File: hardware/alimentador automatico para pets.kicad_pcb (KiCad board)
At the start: 2 copper layers, 96 x 90 mm, 31 parts, among them J1 Conn_01x02, J2 Conn_01x04, J3 Conn_01x03, J4 Conn_01x03, J5 Conn_01x02, J6 Conn_01x05, J7 Conn_01x02, J8 Conn_01x04, Q1 BC337, SW1 SW_Push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

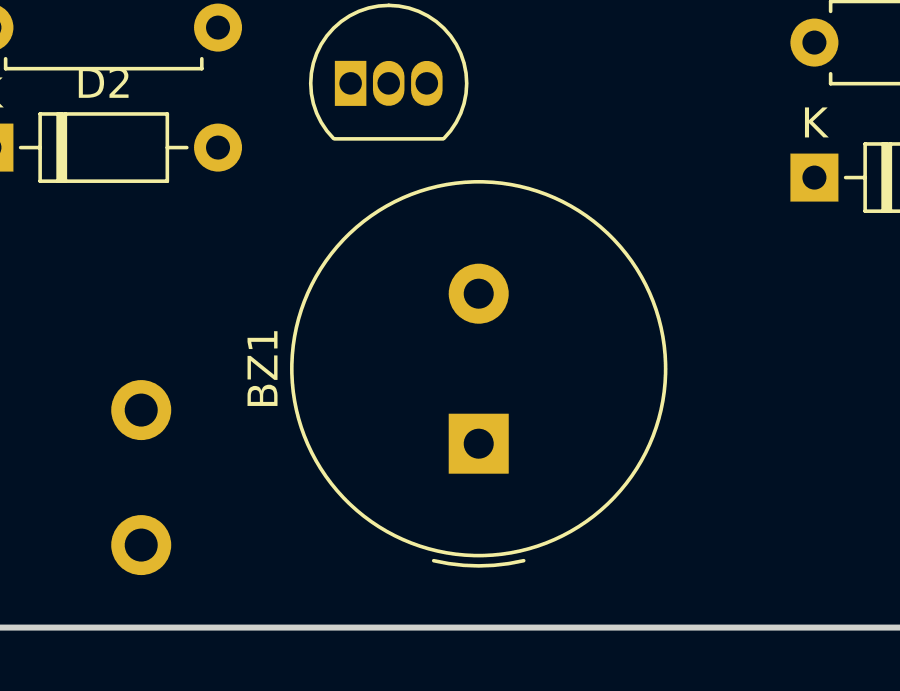
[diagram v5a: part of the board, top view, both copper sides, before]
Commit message: add 3d models pins #14
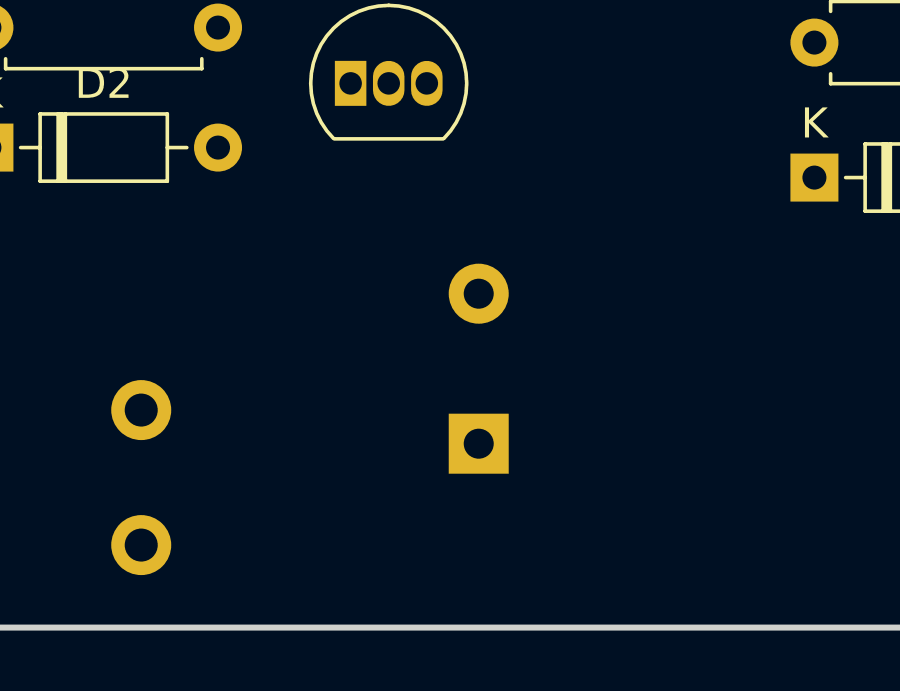
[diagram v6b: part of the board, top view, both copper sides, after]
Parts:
- BZ1: moved to B.Cu
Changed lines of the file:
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@@
-    )
-  )
-  (footprint "Buzzer_Beeper:Buzzer_TDK_PS1240P02BT_D12.2mm_H6.5mm" (layer "F.Cu")
-    (at 89.5 108.870785 90)
-    (descr "Buzzer, D12.2mm height 6.5mm, https://product.tdk.com/info/en/catalog/datasheets/piezoelectronic_buzzer_ps_en.pdf")
-    (tags "buzzer")
-    (property "Sheetfile" "alimentador automatico para pets.kicad_sch")
-    (property "Sheetname" "")
-    (attr through_hole)
-    (fp_text reference "BZ1" (at 2.5 -7.17 90) (layer "F.SilkS")
-      (effects (font (size 1 1) (thickness 0.15)))
-    )
-    (fp_text value "Buzzer" (at 2.5 7.31 90) (layer "F.Fab")
-      (effects (font (size 1 1) (thickness 0.15)))
-    )
-    (fp_text user "${REFERENCE}" (at 2.5 -2.43 90) (layer "F.Fab")
-      (effects (font (size 1 1) (thickness 0.15)))
-    )
-    (fp_arc (start -3.9 1.499999) (mid -4.073431 -0.000001) (end -3.9 -1.5) (layer "F.SilkS") (width 0.12))
-    (fp_circle (center 2.5 0) (end 8.73 0) (layer "F.SilkS") (width 0.12) (fill none))
-    (fp_circle (center 2.5 0) (end 8.85 0) (layer "F.CrtYd") (width 0.05) (fill none))
-    (fp_line (start -1.3 -1) (end -1.3 1) (layer "F.Fab") (width 0.1))
-    (fp_circle (center 2.5 0) (end 3.5 0) (layer "F.Fab") (width 0.1) (fill none))
-    (fp_circle (center 2.5 0) (end 8.6 0) (layer "F.Fab") (width 0.1) (fill none))
-    (pad "1" thru_hole rect (at 0 0 90) (size 2 2) (drill 1) (layers *.Cu *.Mask)
-      (net 1 "/5V") (pinfunction "-") (pintype "passive"))
-    (pad "2" thru_hole circle (at 5 0 90) (size 2 2) (drill 1) (layers *.Cu *.Mask)
-      (net 8 "Net-(BZ1-Pad2)") (pinfunction "+") (pintype "passive"))
-    (model "${KICAD6_3DMODEL_DIR}/Buzzer_Beeper.3dshapes/Buzzer_TDK_PS1240P02BT_D12.2mm_H6.5mm.wrl"
-      (offset (xyz 0 0 0))
-      (scale (xyz 1 1 1))
-      (rotate (xyz 0 0 0))
     )
   )
@@
       (net 13 "/red_wire") (pinfunction "+E") (pintype "input"))
     (model "${KIPRJMOD}/3d_models/HX711.STEP"
-      (offset (xyz 18 10.5 2))
+      (offset (xyz 18.5 10.3 2.5))
       (scale (xyz 1 1 1))
       (rotate (xyz 0 0 180))
+    )
+    (model "${KICAD6_3DMODEL_DIR}/Connector_PinHeader_2.54mm.3dshapes/PinHeader_1x04_P2.54mm_Vertical.step"
+      (offset (xyz -11 4 2.5))
+      (scale (xyz 1 1 1))
+      (rotate (xyz 0 -180 0))
+    )
+    (model "${KICAD6_3DMODEL_DIR}/Connector_PinHeader_2.54mm.3dshapes/PinHeader_1x06_P2.54mm_Vertical.step"
+      (offset (xyz 14 6.3 2))
+      (scale (xyz 1 1 1))
+      (rotate (xyz 0 180 0))
     )
   )
@@
     )
   )
+  (footprint "Buzzer_Beeper:Buzzer_TDK_PS1240P02BT_D12.2mm_H6.5mm" (layer "B.Cu")
+    (at 89.5 108.870785 90)
+    (descr "Buzzer, D12.2mm height 6.5mm, https://product.tdk.com/info/en/catalog/datasheets/piezoelectronic_buzzer_ps_en.pdf")
+    (tags "buzzer")
+    (property "Sheetfile" "alimentador automatico para pets.kicad_sch")
+    (property "Sheetname" "")
+    (attr through_hole)
+    (fp_text reference "BZ1" (at 2.5 7.17 90) (layer "B.SilkS")
+      (effects (font (size 1 1) (thickness 0.15)) (justify mirror))
+    )
+    (fp_text value "Buzzer" (at 2.5 -7.31 90) (layer "B.Fab")
+      (effects (font (size 1 1) (thickness 0.15)) (justify mirror))
+    )
+    (fp_text user "${REFERENCE}" (at 2.5 2.43 90) (layer "B.Fab")
+      (effects (font (size 1 1) (thickness 0.15)) (justify mirror))
+    )
+    (fp_arc (start -3.9 1.5) (mid -4.073431 0.000001) (end -3.9 -1.499999) (layer "B.SilkS") (width 0.12))
+    (fp_circle (center 2.5 0) (end 8.73 0) (layer "B.SilkS") (width 0.12) (fill none))
+    (fp_circle (center 2.5 0) (end 8.85 0) (layer "B.CrtYd") (width 0.05) (fill none))
+    (fp_line (start -1.3 1) (end -1.3 -1) (layer "B.Fab") (width 0.1))
+    (fp_circle (center 2.5 0) (end 3.5 0) (layer "B.Fab") (width 0.1) (fill none))
+    (fp_circle (center 2.5 0) (end 8.6 0) (layer "B.Fab") (width 0.1) (fill none))
+    (pad "1" thru_hole rect (at 0 0 90) (size 2 2) (drill 1) (layers *.Cu *.Mask)
+      (net 1 "/5V") (pinfunction "-") (pintype "passive"))
+    (pad "2" thru_hole circle (at 5 0 90) (size 2 2) (drill 1) (layers *.Cu *.Mask)
+      (net 8 "Net-(BZ1-Pad2)") (pinfunction "+") (pintype "passive"))
+    (model "${KICAD6_3DMODEL_DIR}/Buzzer_Beeper.3dshapes/Buzzer_TDK_PS1240P02BT_D12.2mm_H6.5mm.wrl"
+      (offset (xyz 0 0 0))
+      (scale (xyz 1 1 1))
+      (rotate (xyz 0 0 0))
+    )
+  )
   (footprint "Button_Switch_THT:SW_PUSH_6mm" (layer "B.Cu")
     (at 53.25 107.75 180)
@@
     (effects (font (size 1.5 1.5) (thickness 0.3)))
   )
+  (dimension (type aligned) (layer "Edge.Cuts")
+    (pts (xy 38.5 99.25) (xy 38.5 103))
+    (height 0)
+    (gr_text "3.7500 mm" (at 37.35 101.125 90) (layer "Edge.Cuts")
+      (effects (font (size 1 1) (thickness 0.15)))
+    )
+    (format (units 3) (units_format 1) (precision 4))
+    (style (thickness 0.1) (arrow_length 1.27) (text_position_mode 0) (extension_height 0.58642) (extension_offset 0.5) keep_text_aligned)
+  )
   (via (at 115 110) (size 5) (drill 3) (layers "F.Cu" "B.Cu") (free) (net 2))

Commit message: place components and board roadmap #22
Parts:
- added G***: LOGO, footprint_lib:parafuso, F.Cu at (111.0, 102.0)
- added G***: LOGO, footprint_lib:parafuso, F.Cu at (27.0, 102.0)
- added G***: LOGO, footprint_lib:parafuso, F.Cu at (26.0, 30.0)
- added G***: LOGO, footprint_lib:parafuso, F.Cu at (111.0, 30.0)
- added G***: LOGO, footprint_lib:danger, B.Cu at (35.0, 40.8)
- Q1: footprint Package_TO_SOT_THT:TO-92_Inline -> Package_TO_SOT_THT:TO-92L_Inline_Wide
- moved D3 71.7 mm to (51.0, 28.4), turned to -90 degrees
- moved D2 52.7 mm to (84.5, 47.6), turned to 90 degrees
- moved R1 50.0 mm to (89.0, 47.6), turned to 90 degrees
- moved R4 45.1 mm to (89.0, 50.2), turned to -90 degrees
- moved R6 44.9 mm to (93.5, 39.9), turned to -90 degrees
- moved D1 36.9 mm to (93.5, 50.2), turned to -90 degrees
- moved R5 32.9 mm to (84.5, 57.8), turned to 90 degrees
- moved R2 29.6 mm to (109.0, 82.0)
- moved R3 20.1 mm to (64.2, 69.0)
- moved J7 18.2 mm to (26.2, 59.0), turned to 0 degrees
- moved C1 15.7 mm to (56.1, 60.2), turned to -90 degrees
- moved Q1 14.7 mm to (98.7, 102.8)
- moved SW2 14.6 mm to (66.0, 99.8)
- moved SW1 14.2 mm to (77.5, 99.8)
- moved C2 13.1 mm to (66.0, 59.7), turned to -90 degrees
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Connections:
- J7 pad 1: Net-(J7-Pad1) -> Net-(U3-Pad4)
- J7 pad 2: Net-(J7-Pad2) -> Net-(U3-Pad5)
- U3 pad 4: Net-(J7-Pad2) -> Net-(U3-Pad4)
- U3 pad 5: Net-(J7-Pad1) -> Net-(U3-Pad5)
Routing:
- net GND: track 0.00 -> 273.0 mm, vias 4 -> 3
- net /5V: track 0.00 -> 159.2 mm
- net /3V3: track 0.00 -> 96.5 mm, vias 0 -> 1
- net /BUTTON_3: track 0.00 -> 81.5 mm
- net /SCL_disp: track 0.00 -> 71.7 mm, vias 0 -> 2
- net /SDA_disp: track 0.00 -> 70.1 mm, vias 0 -> 1
- net /BUTTON_2: track 0.00 -> 68.6 mm
- net /DT: track 0.00 -> 65.3 mm
- net /SCK: track 0.00 -> 59.8 mm, vias 0 -> 1
- net /BUTTON_1: track 0.00 -> 55.8 mm
- net Net-(R1-Pad2): track 0.00 -> 51.3 mm, vias 0 -> 1
- net /sMotor: track 0.00 -> 48.1 mm, vias 0 -> 1
- net /+Vcc: track 0.00 -> 46.9 mm
- net /buzzer: track 0.00 -> 43.5 mm, vias 0 -> 1
- net /CLK_encoder: track 0.00 -> 41.1 mm
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- added copper zone on B.Cu, net (none)
- added copper zone on F.Cu, net (none)
- added copper zone on B.Cu, net GND
- added copper zone on F.Cu, net GND
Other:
- board size 96 x 90 mm -> 96 x 82.5 mm
- board text added: "+"
- board text added: "-"
- board text added: "B"
- board text added: "Bat"
- board text added: "G"
- board text added: "Load cell"
- board text added: "R"
- board text added: "W"

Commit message: pcb design review
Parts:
- removed D3: 1N4007, Diode_THT:D_DO-41_SOD81_P10.16mm_Horizontal
- moved C2 1.25 mm to (64.8, 59.7)
- moved C1 1.00 mm to (56.1, 61.2)
- moved R3 1.00 mm to (65.2, 69.0)
- moved G*** 0.28 mm to (29.8, 49.2)
- moved D4 0.25 mm to (97.7, 97.2)
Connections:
- U3 pad 1: Net-(D3-Pad1) -> /5V
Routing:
- net GND: track 273.0 -> 4.35 mm
- net /5V: track 159.2 -> 186.2 mm
- net Net-(D3-Pad1): track 21.6 -> 0.00 mm
- net /SCL_disp: track 71.7 -> 67.4 mm
- net /SDA_disp: track 70.1 -> 66.3 mm
- net /sMotor: track 48.1 -> 51.0 mm
- net /3V3: track 96.5 -> 94.9 mm
- net Net-(R1-Pad2): track 51.3 -> 49.8 mm
- net Net-(R3-Pad2): track 40.0 -> 39.1 mm
- net /ac_check: track 24.1 -> 23.4 mm
- net /SCK: track 59.8 -> 59.3 mm
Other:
- board text added: "Encoder"
- board text added: "IR sensor"
- board text added: "LCD Display"
- board text added: "Motor"
